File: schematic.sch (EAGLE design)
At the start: 8 parts

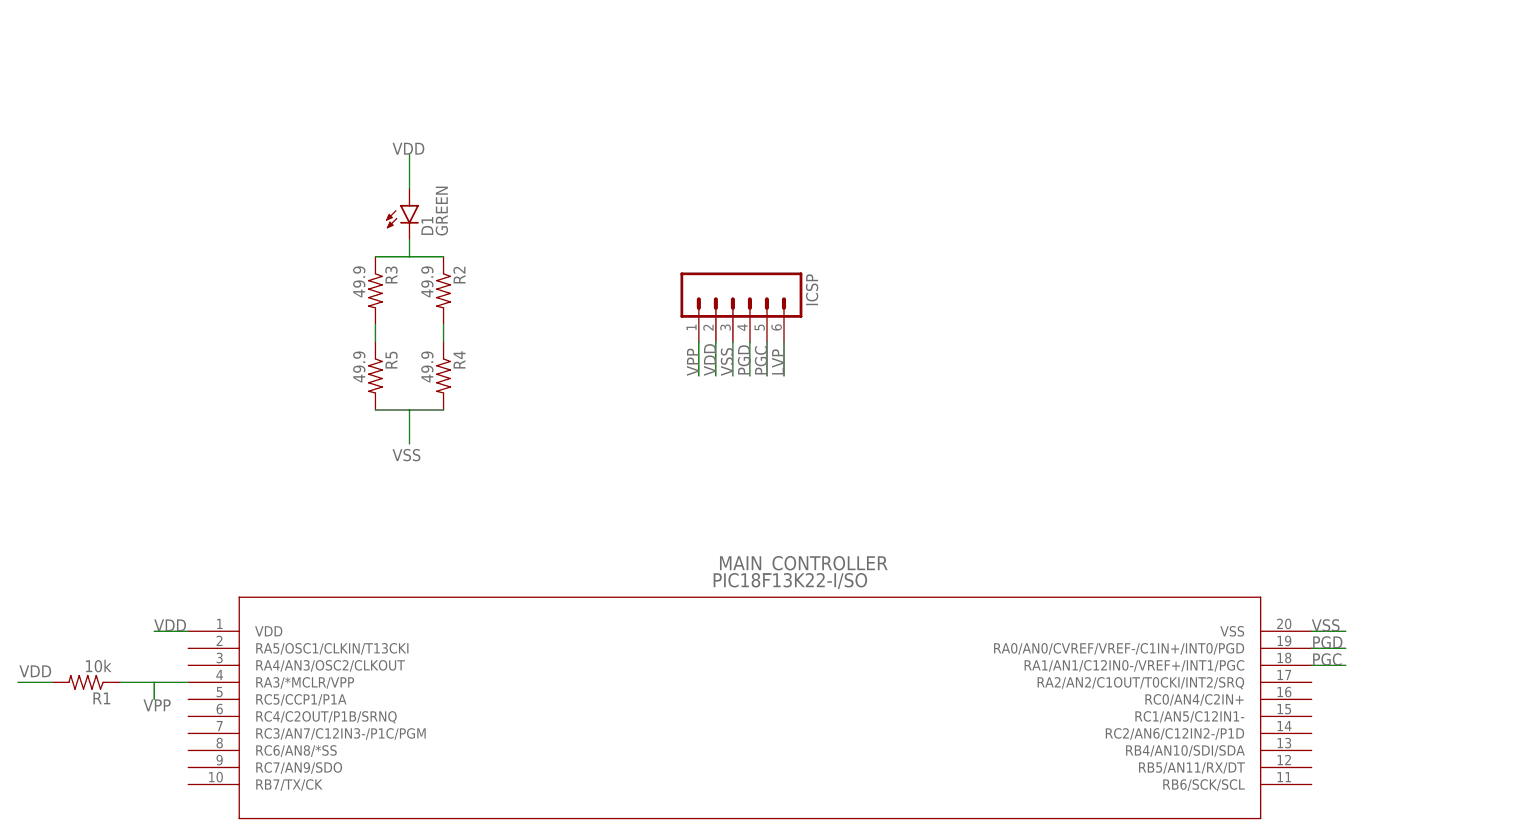
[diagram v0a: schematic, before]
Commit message: Created schematic for ccentral processor and PWM IO
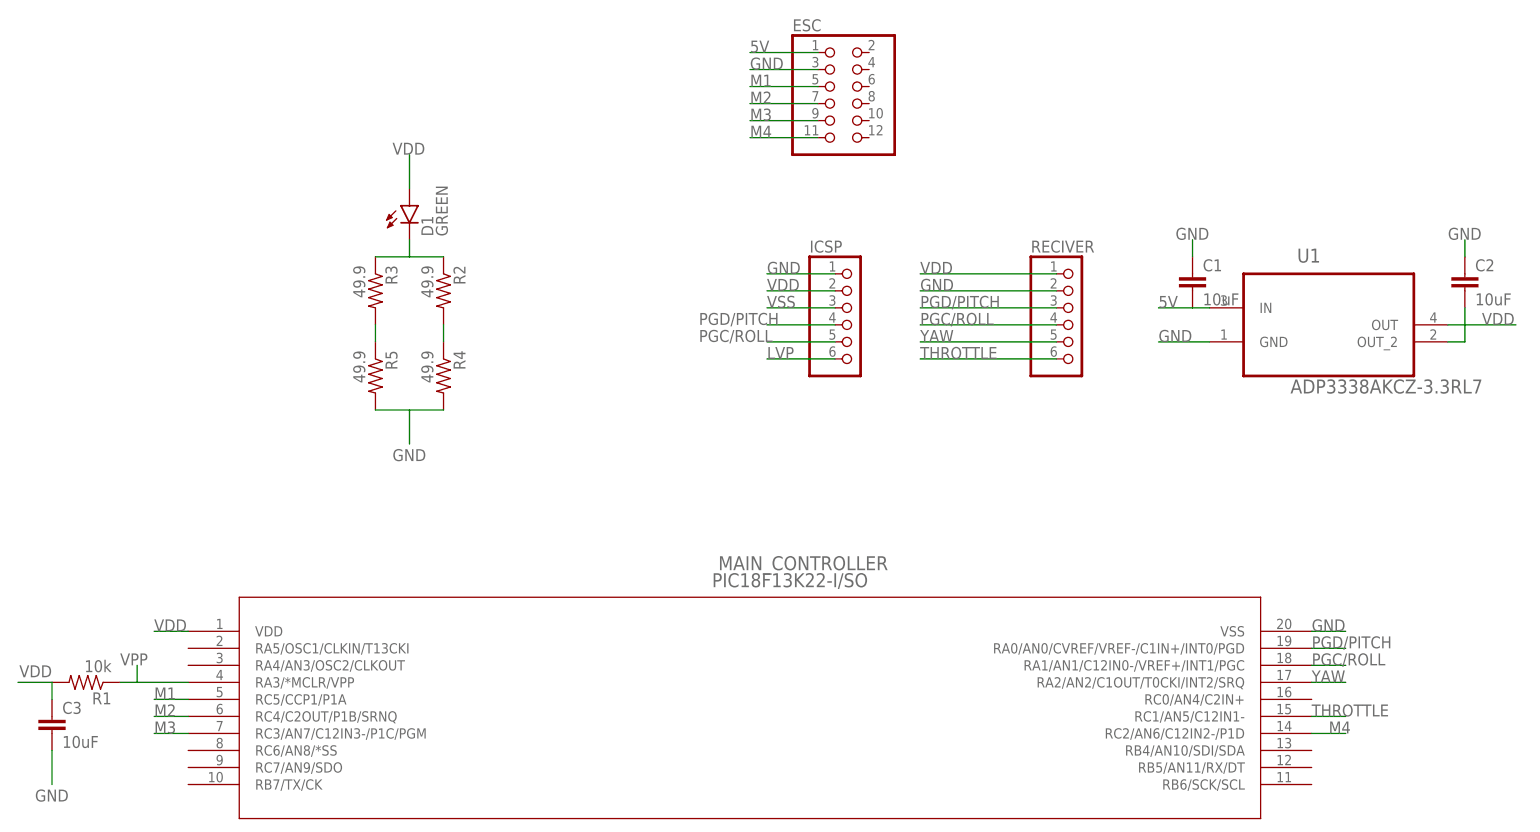
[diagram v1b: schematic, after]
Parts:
- added C1, C2, C3: 10uF, SparkFun-Capacitors:10UF50V20%(1210)
- added ESC: (no value), pinhead:PINHD-2X6
- added RECIVER: (no value), pinhead:PINHD-1X6
- added U1: ADP3338AKCZ-3.3RL7, ADP3338AKCZ-3.3RL7:ADP3338AKCZ-3.3RL7
- ICSP: device SparkFun-Connectors:M06LONGPADS -> pinhead:PINHD-1X6/90
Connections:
- removed net PGC: ICSP.5, MAIN_CONTROLLER.RA1/AN1/C12IN0-/VREF+/INT1/PGC
- removed net PGD: ICSP.4, MAIN_CONTROLLER.RA0/AN0/CVREF/VREF-/C1IN+/INT0/PGD
- new net 5V: C1.2, ESC.1, U1.IN
- new net GND: C1.1, C2.1, C3.2, ESC.3, ICSP.1, MAIN_CONTROLLER.VSS, R4.2, R5.2, RECIVER.2, U1.GND
- new net M1: ESC.5, MAIN_CONTROLLER.RC5/CCP1/P1A
- new net M2: ESC.7, MAIN_CONTROLLER.RC4/C2OUT/P1B/SRNQ
- new net M3: ESC.9, MAIN_CONTROLLER.RC3/AN7/C12IN3-/P1C/PGM
- new net M4: ESC.11, MAIN_CONTROLLER.RC2/AN6/C12IN2-/P1D
- new net PGC/ROLL: ICSP.5, MAIN_CONTROLLER.RA1/AN1/C12IN0-/VREF+/INT1/PGC, RECIVER.4
- new net PGD/PITCH: ICSP.4, MAIN_CONTROLLER.RA0/AN0/CVREF/VREF-/C1IN+/INT0/PGD, RECIVER.3
- new net THROTTLE: MAIN_CONTROLLER.RC1/AN5/C12IN1-, RECIVER.6
- new net YAW: MAIN_CONTROLLER.RA2/AN2/C1OUT/T0CKI/INT2/SRQ, RECIVER.5
- net VDD: now also C2.2, C3.1, RECIVER.1, U1.OUT, U1.OUT_2
- net VPP: no longer ICSP.1
- net VSS: no longer MAIN_CONTROLLER.VSS, R4.2, R5.2

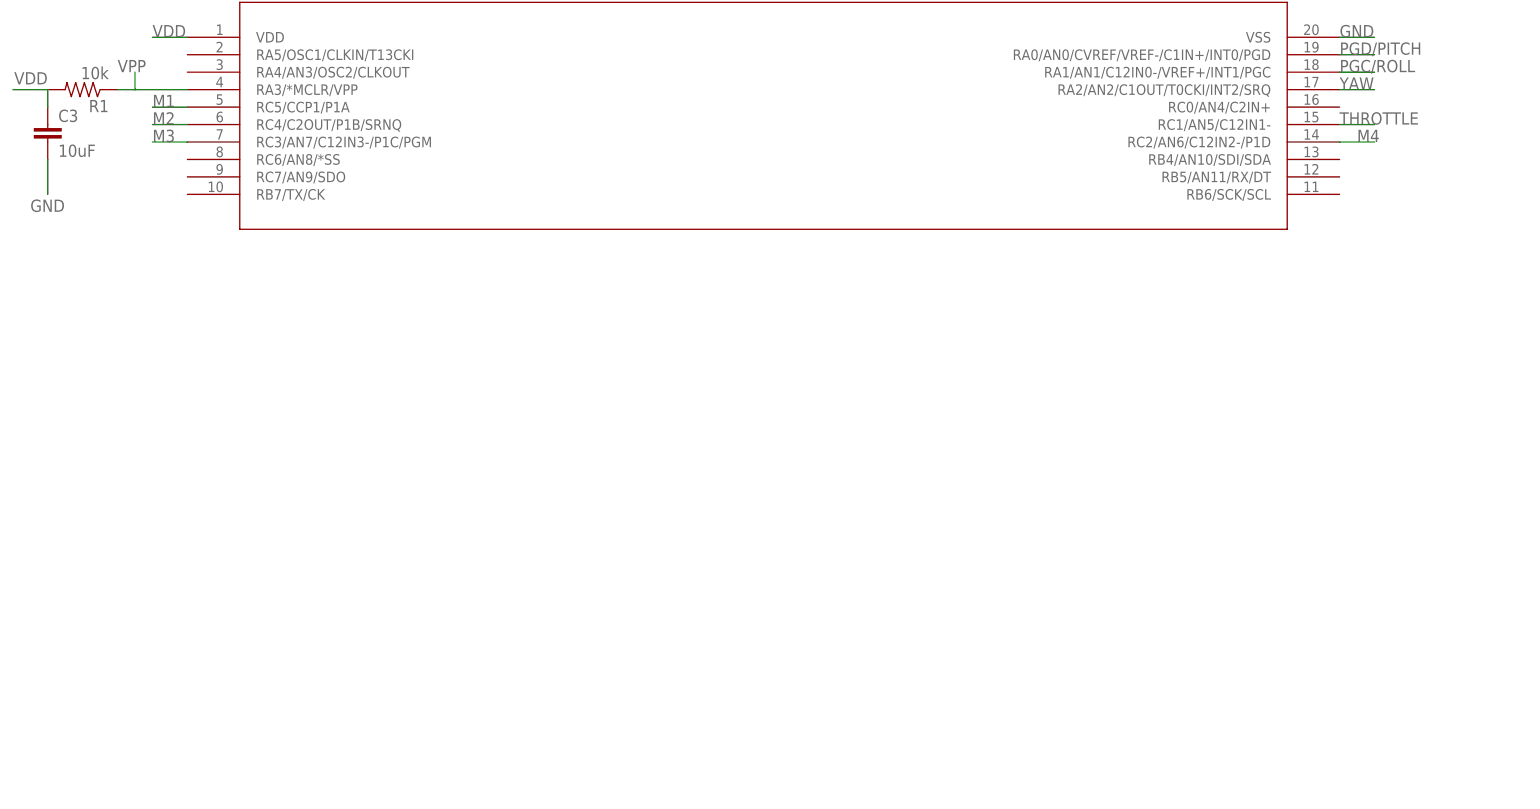
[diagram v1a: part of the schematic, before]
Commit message: Attached IMU and XBEE in schematic. Schematic is now done unless the extra outputs from the xbee are needed
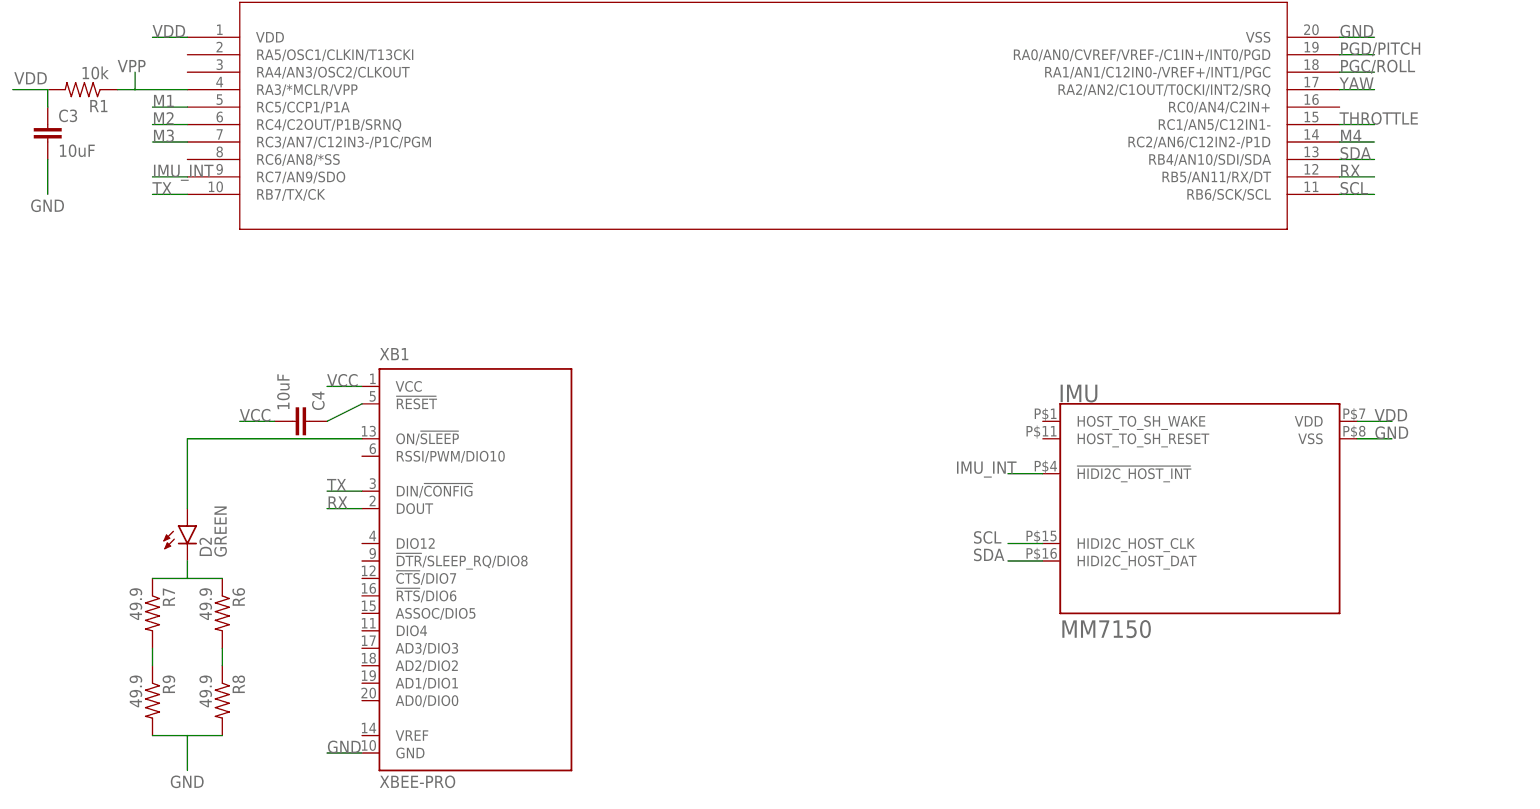
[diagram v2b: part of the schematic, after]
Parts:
- added C4: 10uF, SparkFun-Capacitors:10UF50V20%(1210)
- added D2: GREEN, SparkFun-LED:LED-GREEN1206
- added IMU: MM7150, MM7150:MM7150
- added R6, R7, R8, R9: 49.9, SparkFun-Passives:RESISTOR0402-RES
- added XB1: XBEE-PRO, xbee:XBEE-PRO
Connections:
- new net IMU_INT: IMU.!HIDI2C_HOST_INT, MAIN_CONTROLLER.RC7/AN9/SDO
- new net N$5: C4.1, XB1.!RESET
- new net N$6: R7.2, R9.1
- new net N$7: R6.2, R8.1
- new net N$8: D2.C, R6.1, R7.1
- new net N$9: D2.A, XB1.ON/!SLEEP
- new net RX: MAIN_CONTROLLER.RB5/AN11/RX/DT, XB1.DOUT
- new net SCL: IMU.HIDI2C_HOST_CLK, MAIN_CONTROLLER.RB6/SCK/SCL
- new net SDA: IMU.HIDI2C_HOST_DAT, MAIN_CONTROLLER.RB4/AN10/SDI/SDA
- new net TX: MAIN_CONTROLLER.RB7/TX/CK, XB1.DIN/!CONFIG
- new net VCC: C4.2, XB1.VCC
- net GND: now also IMU.VSS, R8.2, R9.2, XB1.GND
- net VDD: now also IMU.VDD
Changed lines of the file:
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@@
 <part name="C2" library="SparkFun-Capacitors" deviceset="10UF50V20%(1210)" device="" value="10uF"/>
 <part name="C3" library="SparkFun-Capacitors" deviceset="10UF50V20%(1210)" device="" value="10uF"/>
+<part name="IMU" library="MM7150" deviceset="MM7150" device=""/>
+<part name="XB1" library="xbee" deviceset="XBEE" device="-PRO"/>
+<part name="C4" library="SparkFun-Capacitors" deviceset="10UF50V20%(1210)" device="" value="10uF"/>
+<part name="D2" library="SparkFun-LED" deviceset="LED-GREEN" device="1206" value="GREEN"/>
+<part name="R6" library="SparkFun-Passives" deviceset="RESISTOR" device="0402-RES" value="49.9"/>
+<part name="R7" library="SparkFun-Passives" deviceset="RESISTOR" device="0402-RES" value="49.9"/>
+<part name="R8" library="SparkFun-Passives" deviceset="RESISTOR" device="0402-RES" value="49.9"/>
+<part name="R9" library="SparkFun-Passives" deviceset="RESISTOR" device="0402-RES" value="49.9"/>
 </parts>
 <sheets>
@@
 <instance part="C2" gate="G$1" x="190.5" y="50.8"/>
 <instance part="C3" gate="G$1" x="-20.32" y="-15.24"/>
+<instance part="IMU" gate="A" x="147.32" y="-68.58"/>
+<instance part="XB1" gate="G$1" x="40.64" y="-76.2"/>
+<instance part="C4" gate="G$1" x="15.24" y="-55.88" rot="MR90"/>
+<instance part="D2" gate="G$1" x="0" y="-71.12"/>
+<instance part="R6" gate="G$1" x="5.08" y="-83.82" rot="R270"/>
+<instance part="R7" gate="G$1" x="-5.08" y="-83.82" rot="R270"/>
+<instance part="R8" gate="G$1" x="5.08" y="-96.52" rot="R270"/>
+<instance part="R9" gate="G$1" x="-5.08" y="-96.52" rot="R270"/>
 </instances>
 <busses>
@@
 <label x="109.22" y="53.34" size="1.778" layer="95"/>
 </segment>
+<segment>
+<pinref part="IMU" gate="A" pin="VDD"/>
+<wire x1="170.18" y1="-55.88" x2="175.26" y2="-55.88" width="0.1524" layer="91"/>
+<label x="172.72" y="-55.88" size="1.778" layer="95"/>
+</segment>
 </net>
 <net name="VSS" class="0">
@@
 <label x="187.96" y="58.42" size="1.778" layer="95"/>
 </segment>
+<segment>
+<pinref part="XB1" gate="G$1" pin="GND"/>
+<wire x1="25.4" y1="-104.14" x2="20.32" y2="-104.14" width="0.1524" layer="91"/>
+<label x="20.32" y="-104.14" size="1.778" layer="95"/>
+</segment>
+<segment>
+<pinref part="IMU" gate="A" pin="VSS"/>
+<wire x1="170.18" y1="-58.42" x2="175.26" y2="-58.42" width="0.1524" layer="91"/>
+<label x="172.72" y="-58.42" size="1.778" layer="95"/>
+</segment>
+<segment>
+<pinref part="R8" gate="G$1" pin="2"/>
+<pinref part="R9" gate="G$1" pin="2"/>
+<wire x1="5.08" y1="-101.6" x2="0" y2="-101.6" width="0.1524" layer="91"/>
+<wire x1="0" y1="-101.6" x2="-5.08" y2="-101.6" width="0.1524" layer="91"/>
+<wire x1="0" y1="-101.6" x2="0" y2="-106.68" width="0.1524" layer="91"/>
+<label x="-2.54" y="-109.22" size="1.778" layer="95"/>
+</segment>
 </net>
 <net name="M1" class="0">
@@
 <pinref part="MAIN_CONTROLLER" gate="A" pin="RC2/AN6/C12IN2-/P1D"/>
 <wire x1="167.64" y1="-15.24" x2="172.72" y2="-15.24" width="0.1524" layer="91"/>
-<label x="170.18" y="-15.24" size="1.778" layer="95"/>
+<label x="167.64" y="-15.24" size="1.778" layer="95"/>
 </segment>
 </net>
@@
 </segment>
 </net>
+<net name="VCC" class="0">
+<segment>
+<pinref part="XB1" gate="G$1" pin="VCC"/>
+<wire x1="25.4" y1="-50.8" x2="20.32" y2="-50.8" width="0.1524" layer="91"/>
+<label x="20.32" y="-50.8" size="1.778" layer="95"/>
+</segment>
+<segment>
+<pinref part="C4" gate="G$1" pin="2"/>
+<wire x1="12.7" y1="-55.88" x2="7.62" y2="-55.88" width="0.1524" layer="91"/>
+<label x="7.62" y="-55.88" size="1.778" layer="95"/>
+</segment>
+</net>
+<net name="SCL" class="0">
+<segment>
+<pinref part="MAIN_CONTROLLER" gate="A" pin="RB6/SCK/SCL"/>
+<wire x1="167.64" y1="-22.86" x2="172.72" y2="-22.86" width="0.1524" layer="91"/>
+<label x="167.64" y="-22.86" size="1.778" layer="95"/>
+</segment>
+<segment>
+<pinref part="IMU" gate="A" pin="HIDI2C_HOST_CLK"/>
+<wire x1="124.46" y1="-73.66" x2="119.38" y2="-73.66" width="0.1524" layer="91"/>
+<label x="114.3" y="-73.66" size="1.778" layer="95"/>
+</segment>
+</net>
+<net name="SDA" class="0">
+<segment>
+<pinref part="MAIN_CONTROLLER" gate="A" pin="RB4/AN10/SDI/SDA"/>
+<wire x1="167.64" y1="-17.78" x2="172.72" y2="-17.78" width="0.1524" layer="91"/>
+<label x="167.64" y="-17.78" size="1.778" layer="95"/>
+</segment>
+<segment>
+<pinref part="IMU" gate="A" pin="HIDI2C_HOST_DAT"/>
+<wire x1="124.46" y1="-76.2" x2="119.38" y2="-76.2" width="0.1524" layer="91"/>
+<label x="114.3" y="-76.2" size="1.778" layer="95"/>
+</segment>
+</net>
+<net name="IMU_INT" class="0">
+<segment>
+<pinref part="IMU" gate="A" pin="!HIDI2C_HOST_INT"/>
+<wire x1="124.46" y1="-63.5" x2="119.38" y2="-63.5" width="0.1524" layer="91"/>
+<label x="111.76" y="-63.5" size="1.778" layer="95"/>
+</segment>
+<segment>
+<pinref part="MAIN_CONTROLLER" gate="A" pin="RC7/AN9/SDO"/>
+<wire x1="0" y1="-20.32" x2="-5.08" y2="-20.32" width="0.1524" layer="91"/>
+<label x="-5.08" y="-20.32" size="1.778" layer="95"/>
+</segment>
+</net>
+<net name="TX" class="0">
+<segment>
+<pinref part="MAIN_CONTROLLER" gate="A" pin="RB7/TX/CK"/>
+<wire x1="0" y1="-22.86" x2="-5.08" y2="-22.86" width="0.1524" layer="91"/>
+<label x="-5.08" y="-22.86" size="1.778" layer="95"/>
+</segment>
+<segment>
+<pinref part="XB1" gate="G$1" pin="DIN/!CONFIG"/>
+<wire x1="25.4" y1="-66.04" x2="20.32" y2="-66.04" width="0.1524" layer="91"/>
+<label x="20.32" y="-66.04" size="1.778" layer="95"/>
+</segment>
+</net>
+<net name="RX" class="0">
+<segment>
+<pinref part="MAIN_CONTROLLER" gate="A" pin="RB5/AN11/RX/DT"/>
+<wire x1="167.64" y1="-20.32" x2="172.72" y2="-20.32" width="0.1524" layer="91"/>
+<label x="167.64" y="-20.32" size="1.778" layer="95"/>
+</segment>
+<segment>
+<pinref part="XB1" gate="G$1" pin="DOUT"/>
+<wire x1="25.4" y1="-68.58" x2="20.32" y2="-68.58" width="0.1524" layer="91"/>
+<label x="20.32" y="-68.58" size="1.778" layer="95"/>
+</segment>
+</net>
+<net name="N$5" class="0">
+<segment>
+<pinref part="XB1" gate="G$1" pin="!RESET"/>
+<pinref part="C4" gate="G$1" pin="1"/>
+<wire x1="20.32" y1="-55.88" x2="25.4" y2="-53.34" width="0.1524" layer="91"/>
+</segment>
+</net>
+<net name="N$6" class="0">
+<segment>
+<pinref part="R9" gate="G$1" pin="1"/>
+<pinref part="R7" gate="G$1" pin="2"/>
+<wire x1="-5.08" y1="-91.44" x2="-5.08" y2="-88.9" width="0.1524" layer="91"/>
+</segment>
+</net>
+<net name="N$7" class="0">
+<segment>
+<pinref part="R8" gate="G$1" pin="1"/>
+<pinref part="R6" gate="G$1" pin="2"/>
+<wire x1="5.08" y1="-91.44" x2="5.08" y2="-88.9" width="0.1524" layer="91"/>
+</segment>
+</net>
+<net name="N$8" class="0">
+<segment>
+<pinref part="R6" gate="G$1" pin="1"/>
+<pinref part="D2" gate="G$1" pin="C"/>
+<wire x1="5.08" y1="-78.74" x2="0" y2="-78.74" width="0.1524" layer="91"/>
+<wire x1="0" y1="-78.74" x2="0" y2="-76.2" width="0.1524" layer="91"/>
+<pinref part="R7" gate="G$1" pin="1"/>
+<wire x1="-5.08" y1="-78.74" x2="0" y2="-78.74" width="0.1524" layer="91"/>
+</segment>
+</net>
+<net name="N$9" class="0">
+<segment>
+<pinref part="XB1" gate="G$1" pin="ON/!SLEEP"/>
+<pinref part="D2" gate="G$1" pin="A"/>
+<wire x1="25.4" y1="-58.42" x2="0" y2="-58.42" width="0.1524" layer="91"/>
+<wire x1="0" y1="-58.42" x2="0" y2="-68.58" width="0.1524" layer="91"/>
+</segment>
+</net>
